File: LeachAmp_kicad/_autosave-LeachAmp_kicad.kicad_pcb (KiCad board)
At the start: 2 copper layers, 262.4 x 104.9 mm, 124 parts, among them J1 Conn_01x12_Female, J2 Conn_01x04_Female, J3 Conn_01x03_Female, J4 Conn_01x03_Female, Q1 BC546, Q10 MPSA06, Q11 MPSA56, Q12 BF470, Q13 BF469, Q14 BF469, Q15 BF470, Q16 MJE15030, Q17 MJE15031, Q2 BC546, Q3 BC556, Q4 BC556, Q5 BC546, Q6 BC556, Q8 BC556, Q9 BC546, T1 MJL3281, T2 MJL3201, T3 MJL3281, T4 MJL3201

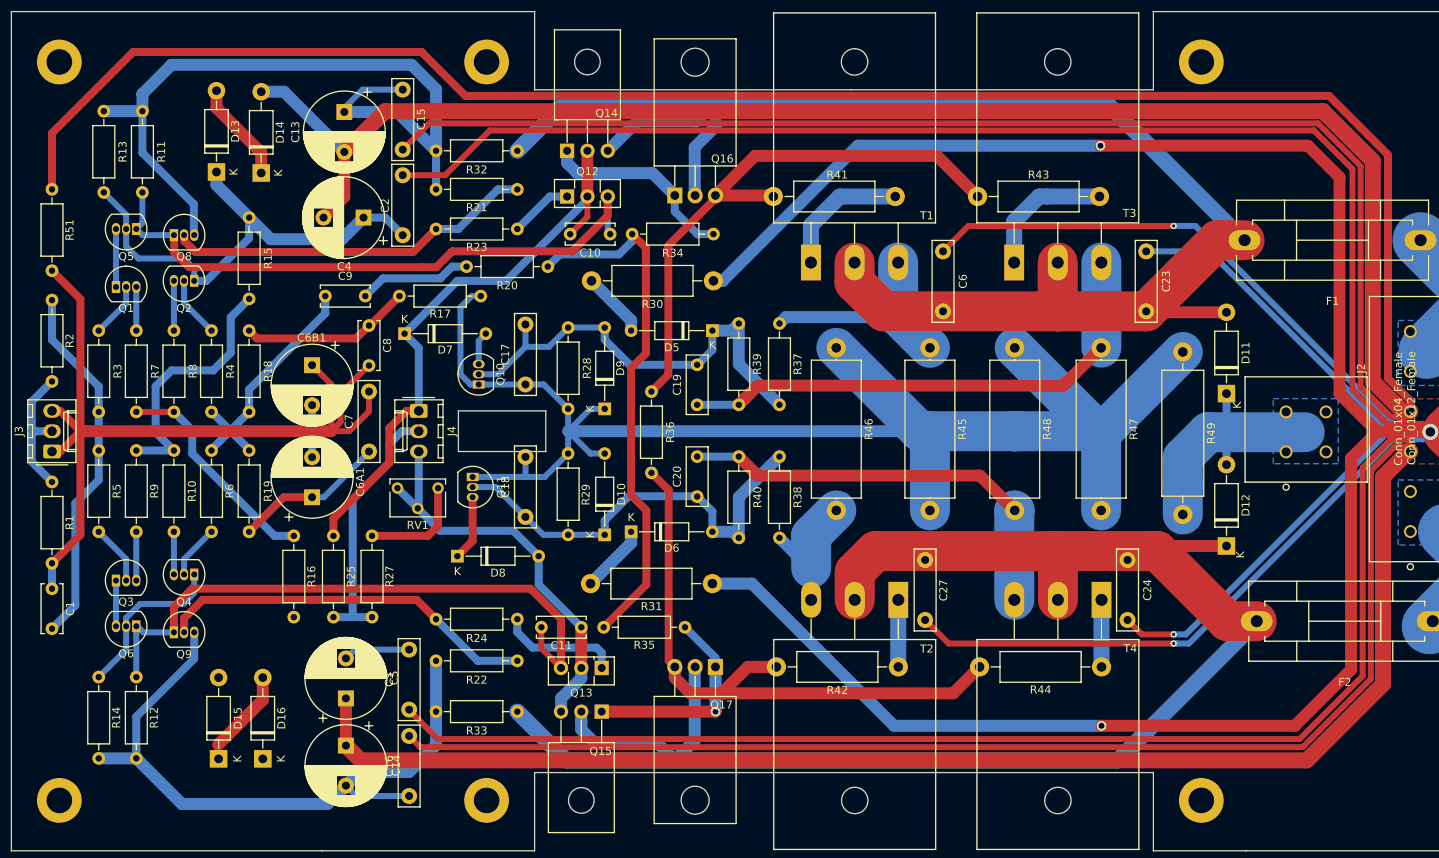
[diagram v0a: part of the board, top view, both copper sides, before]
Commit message: nove_rozmery_soucastek
Nové rozměry součástek hlavně u kondenzátorů
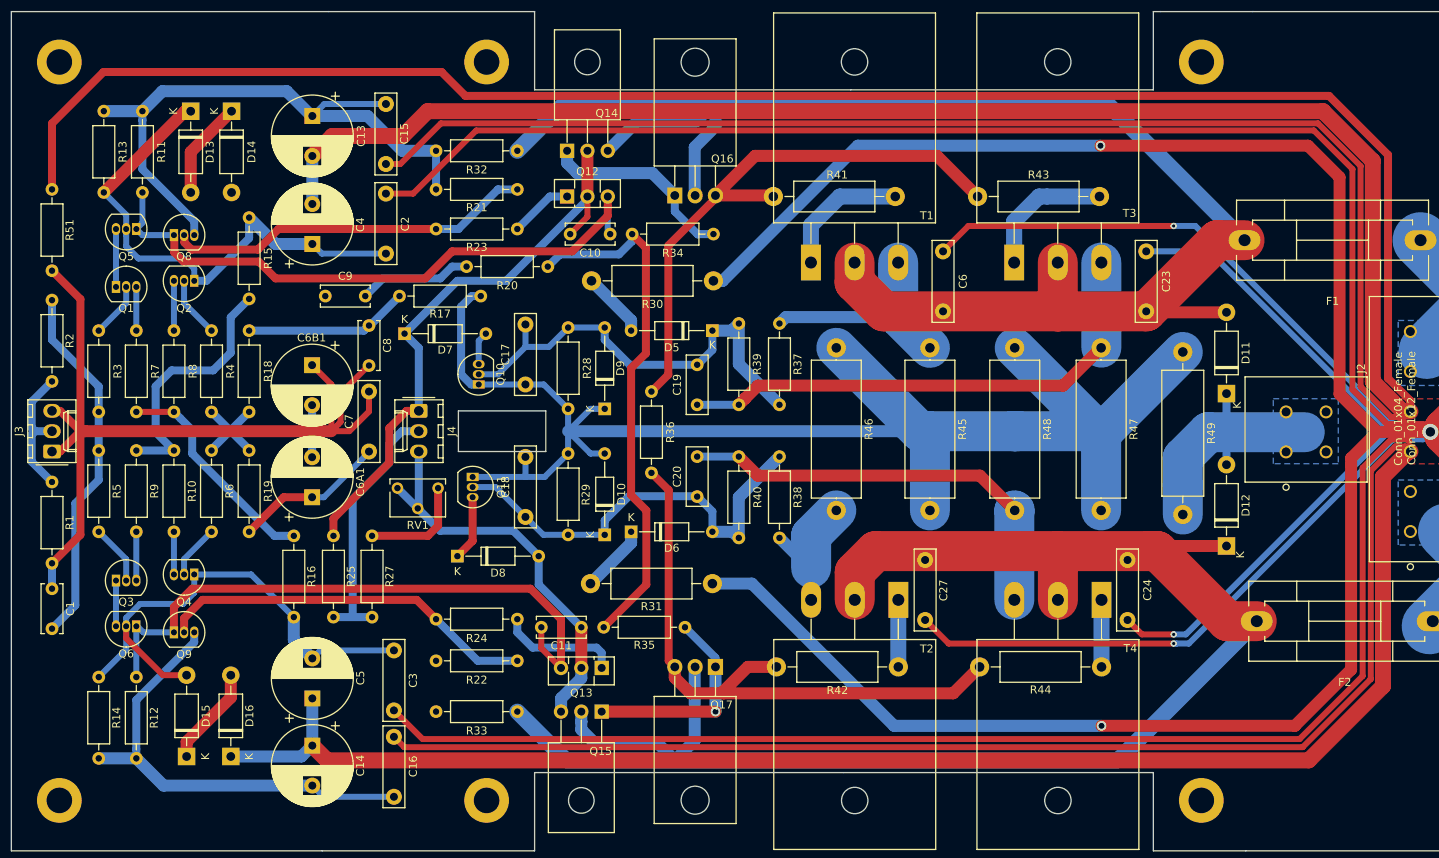
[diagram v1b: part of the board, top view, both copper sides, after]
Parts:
- moved D14 8.57 mm to (99.1, 51.4), turned to 270 degrees
- moved D13 8.26 mm to (94.0, 51.4), turned to 270 degrees
- moved C4 7.20 mm to (109.2, 68.0), turned to 90 degrees
- moved C14 4.20 mm to (109.2, 130.7)
- moved C5 4.20 mm to (109.2, 124.8)
- moved C13 4.03 mm to (109.2, 52.0)
- moved D15 4.01 mm to (93.5, 132.1)
- moved D16 4.01 mm to (99.0, 132.1)
- moved C2 3.11 mm to (118.4, 61.7)
- moved C15 2.77 mm to (118.4, 50.5)
- moved C3 1.90 mm to (119.4, 126.3)
- moved C16 1.90 mm to (119.4, 129.6)
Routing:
- net Net-(C3-Pad2): track 29.4 -> 63.4 mm
- net Net-(C14-Pad2): track 85.3 -> 57.6 mm
- net Net-(C13-Pad1): track 99.8 -> 79.0 mm
- net Net-(C9-Pad1): track 32.0 -> 13.5 mm
- net GND: track 1894.4 -> 1905.3 mm
- net Net-(C2-Pad2): track 60.4 -> 64.7 mm
- net Net-(D15-Pad1): track 10.7 -> 12.4 mm
- net Net-(C10-Pad2): track 77.0 -> 78.2 mm
- net Net-(C8-Pad1): track 21.4 -> 20.7 mm
